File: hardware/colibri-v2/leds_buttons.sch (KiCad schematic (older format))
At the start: 38 parts

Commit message: added wnd_lcd.sch
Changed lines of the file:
@@
 $Descr A4 11693 8268
 encoding utf-8
-Sheet 4 22
+Sheet 4 23
 Title ""
 Date ""
@@
 	3100 2950 3250 2950
 Wire Wire Line
-	3250 2600 3250 2950
-Wire Wire Line
-	3250 2950 3250 3100
+	3250 2600 3250 3100
 $Comp
 L C C?
@@
 	2350 3850 2350 3600
 Wire Wire Line
-	2050 2950 2350 2950
-Wire Wire Line
-	2350 2950 2500 2950
+	2050 2950 2500 2950
 Wire Wire Line
 	2350 3300 2350 2950
@@
 	3100 4750 3250 4750
 Wire Wire Line
-	3250 4400 3250 4750
-Wire Wire Line
-	3250 4750 3250 4900
+	3250 4400 3250 4900
 $Comp
 L C C?
@@
 	2350 5650 2350 5400
 Wire Wire Line
-	2050 4750 2350 4750
-Wire Wire Line
-	2350 4750 2500 4750
+	2050 4750 2500 4750
 Wire Wire Line
 	2350 5100 2350 4750
@@
 	3100 6600 3250 6600
 Wire Wire Line
-	3250 6250 3250 6600
-Wire Wire Line
-	3250 6600 3250 6750
+	3250 6250 3250 6750
 $Comp
 L C C?
@@
 	2350 7500 2350 7250
 Wire Wire Line
-	2050 6600 2350 6600
-Wire Wire Line
-	2350 6600 2500 6600
+	2050 6600 2500 6600
 Wire Wire Line
 	2350 6950 2350 6600
@@
 	6050 2950 6200 2950
 Wire Wire Line
-	6200 2600 6200 2950
-Wire Wire Line
-	6200 2950 6200 3100
+	6200 2600 6200 3100
 $Comp
 L C C?
@@
 	5300 3850 5300 3600
 Wire Wire Line
-	5000 2950 5300 2950
-Wire Wire Line
-	5300 2950 5450 2950
+	5000 2950 5450 2950
 Wire Wire Line
 	5300 3300 5300 2950
@@
 	6050 4750 6200 4750
 Wire Wire Line
-	6200 4400 6200 4750
-Wire Wire Line
-	6200 4750 6200 4900
+	6200 4400 6200 4900
 $Comp
 L C C?
@@
 	5300 5650 5300 5400
 Wire Wire Line
-	5000 4750 5300 4750
-Wire Wire Line
-	5300 4750 5450 4750
+	5000 4750 5450 4750
 Wire Wire Line
 	5300 5100 5300 4750
@@
 	3250 1200 3100 1200
 Wire Wire Line
-	2350 1100 2350 1200
-Wire Wire Line
-	2350 1200 2350 1300
-Wire Wire Line
-	1350 1200 2350 1200
-Wire Wire Line
-	2350 1200 2500 1200
+	2350 1100 2350 1300
+Wire Wire Line
+	1350 1200 2500 1200
 Connection ~ 2350 1200
 Wire Wire Line
@@
 $EndComp
 Wire Wire Line
-	10100 850  10100 1150
-Wire Wire Line
-	10100 1150 10100 1450
-Wire Wire Line
-	10100 1450 10100 1750
-Wire Wire Line
-	10100 1750 10100 1950
+	10100 850  10100 1950
 Wire Wire Line
 	10100 850  9650 850
@@
 	5300 1200 5300 1300
 Wire Wire Line
-	4300 1200 5300 1200
-Wire Wire Line
-	5300 1200 5450 1200
+	4300 1200 5450 1200
 Connection ~ 5300 1200
 Text HLabel 4300 1200 0    60   Output ~ 0

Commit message: Annotated Components
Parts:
- gave numbers to parts that had none: 38

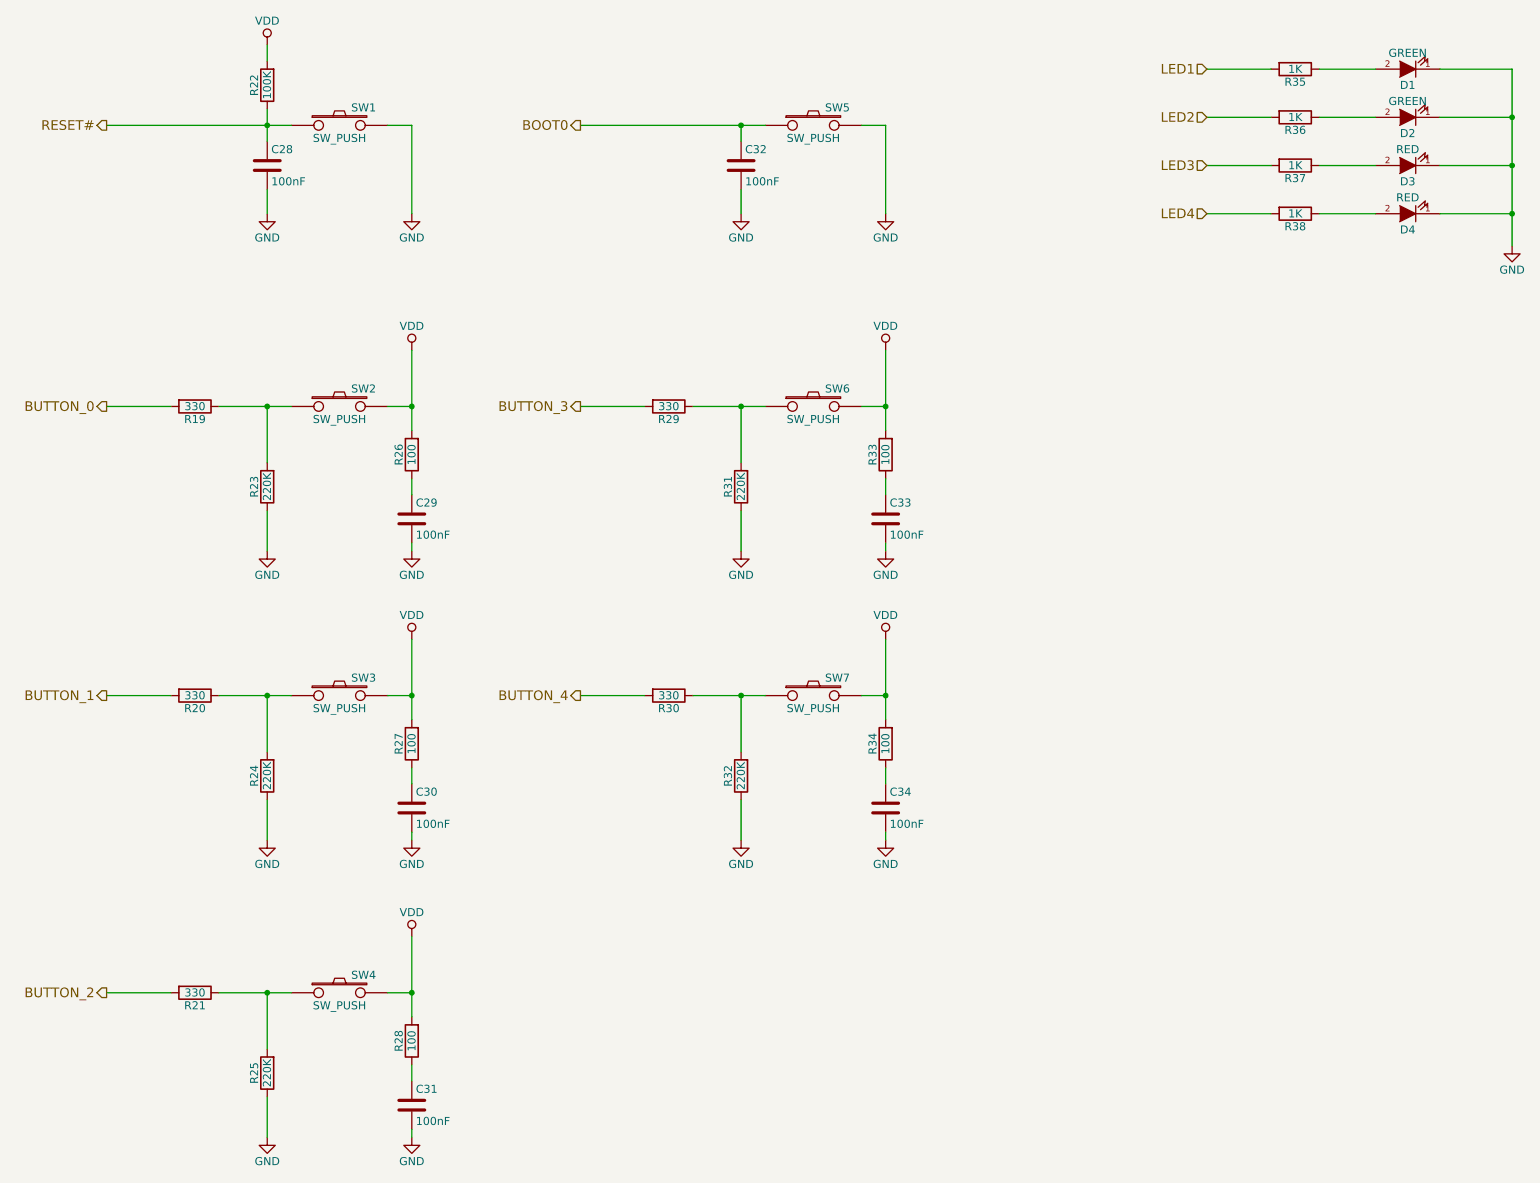
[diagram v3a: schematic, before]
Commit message: Changes in the button sheet
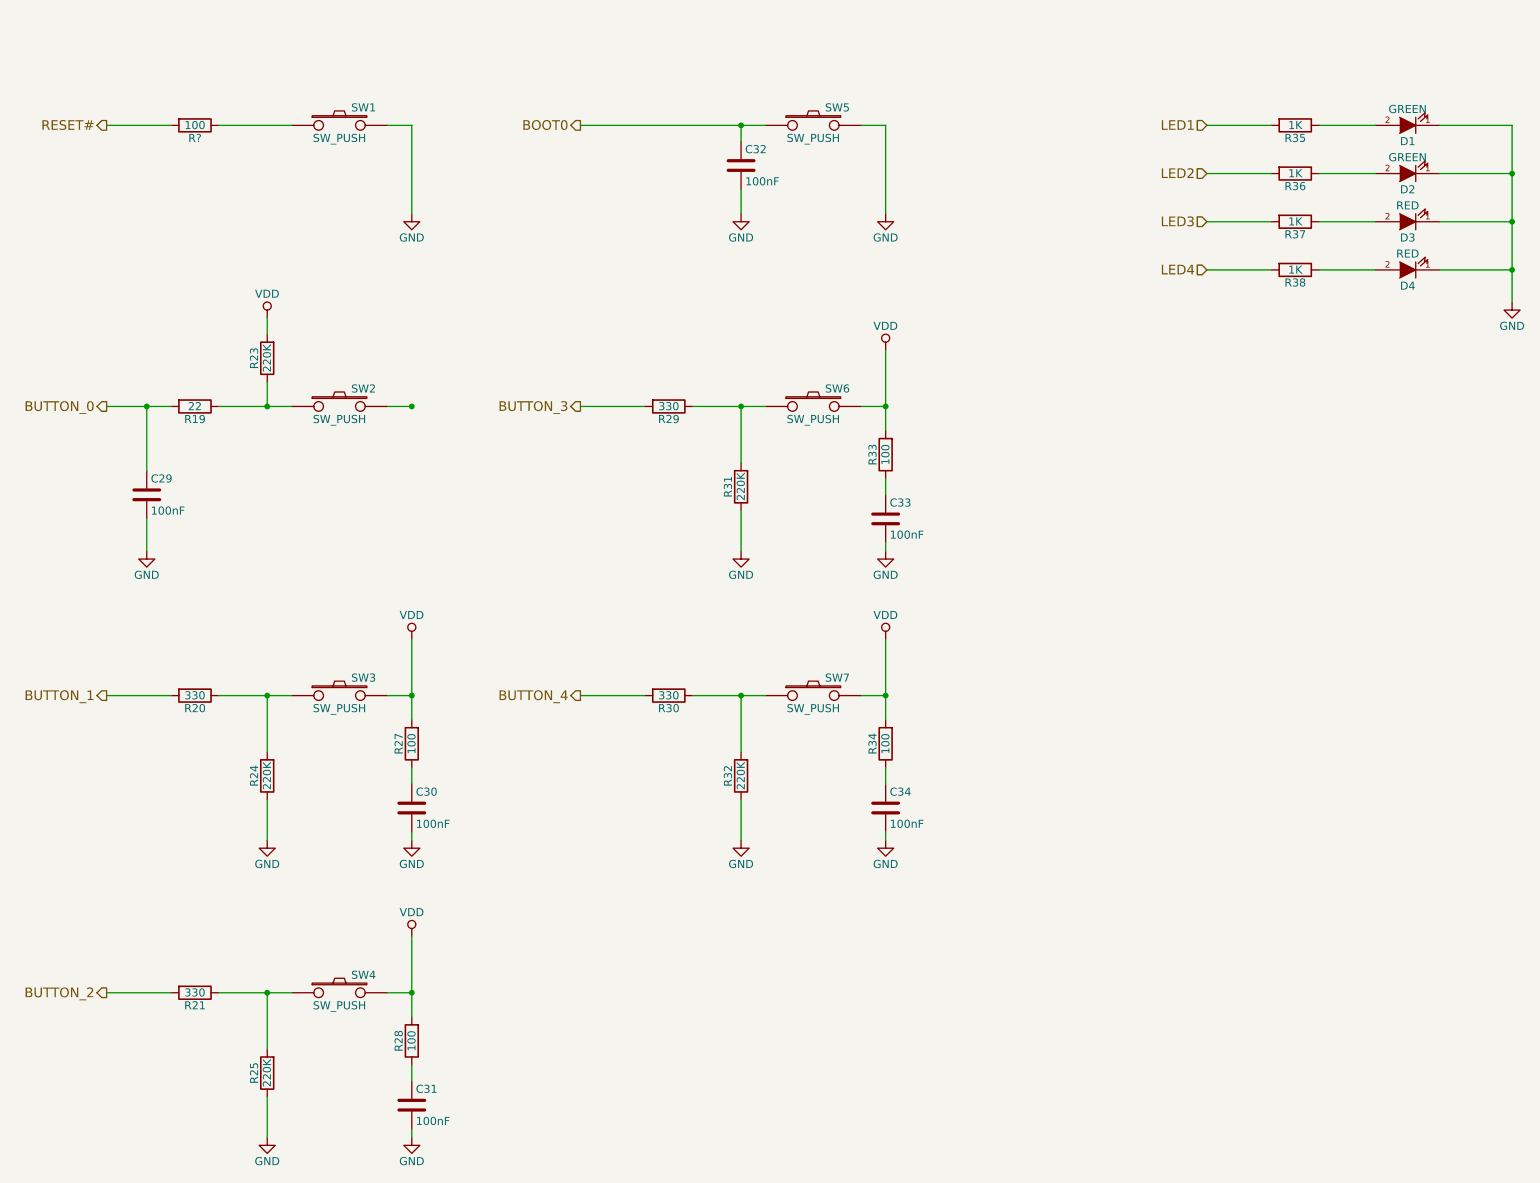
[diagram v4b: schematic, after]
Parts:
- removed C28: 100nF, symbol C
- removed R22: 100K, symbol R
- removed R26: 100, symbol R
- added R?: 100, symbol R
- R19: value 330 -> 22
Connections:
- net BUTTON_0: now also C29.1
- net GND: no longer R23.1
- net RESET#: now also R?.2; no longer SW1.1
- net VDD: now also R23.2; no longer SW2.2
- net at R19.1, SW2.1: now also R23.1; no longer R23.2
- new net: R?.1, SW1.1
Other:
- moved on the sheet: C29, D1, D2, D3, D4, R23, R35, R36, R37, R38

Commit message: Changes the leds
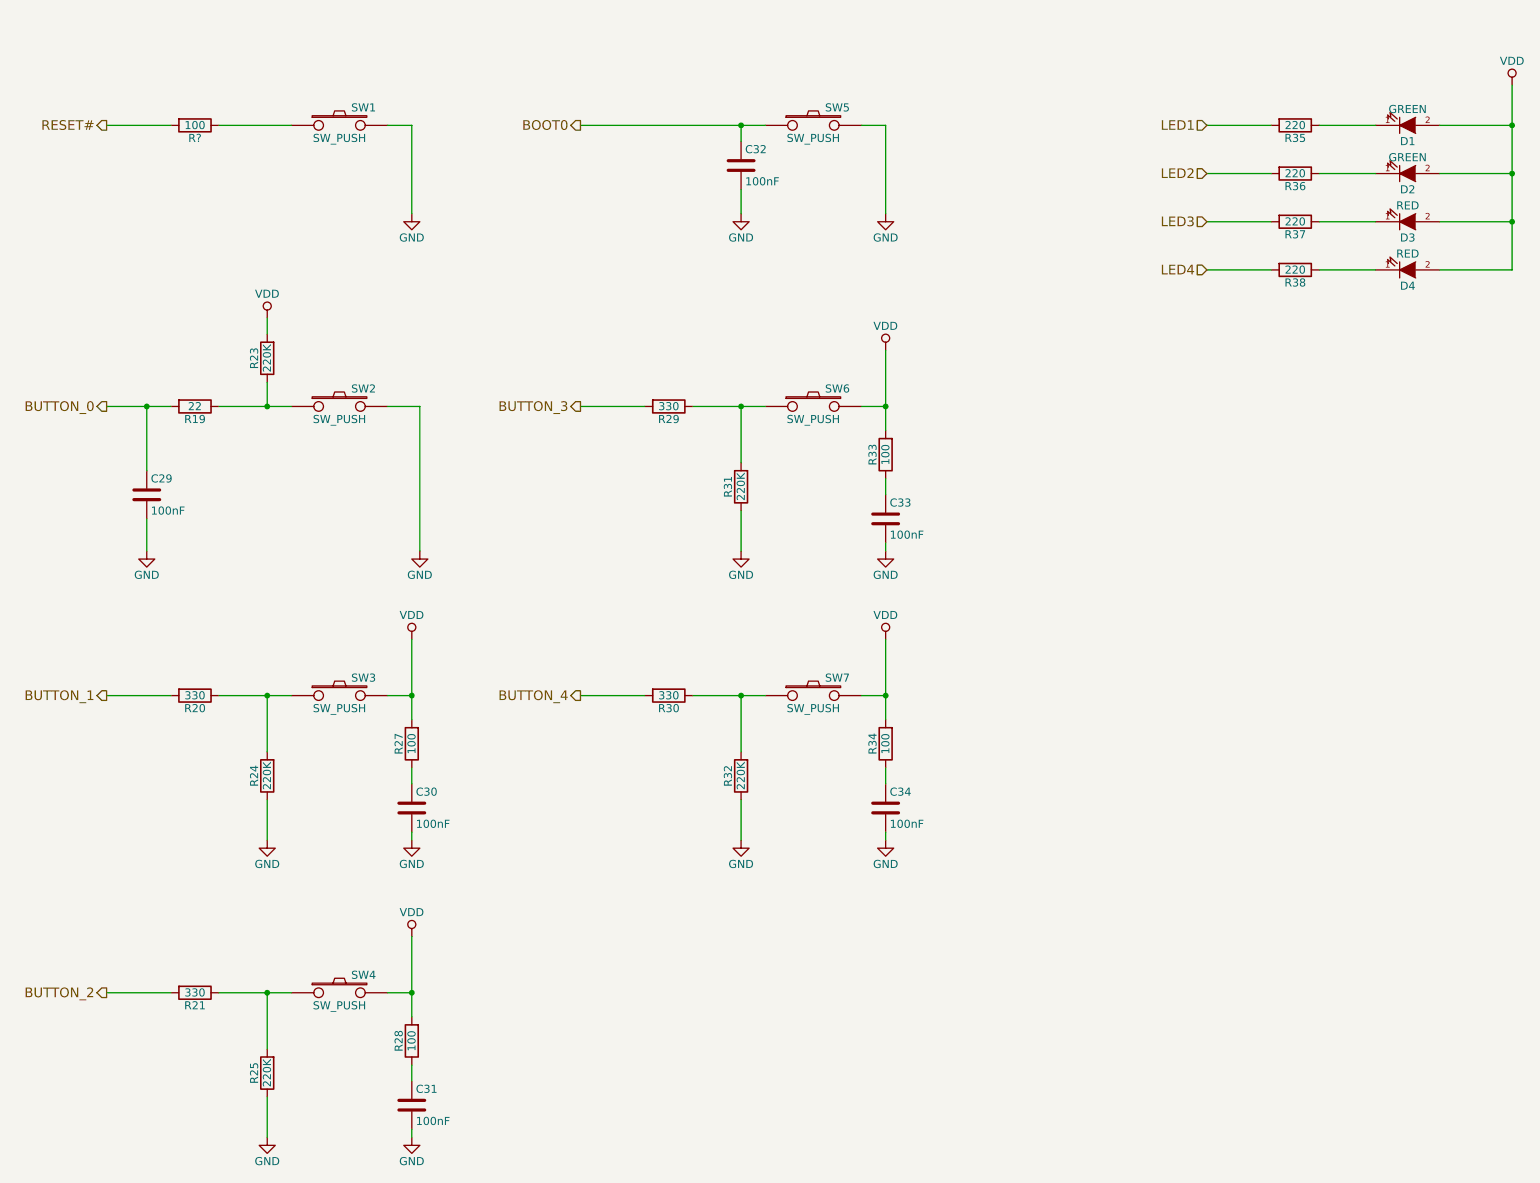
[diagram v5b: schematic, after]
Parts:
- R35, R36, R37, R38: value 1K -> 220
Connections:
- net GND: now also SW2.2; no longer D1.1 (K), D2.1 (K), D3.1 (K), D4.1 (K)
- net VDD: now also D1.2 (A), D2.2 (A), D3.2 (A), D4.2 (A)
- net at R35.1: now also D1.1 (K); no longer D1.2 (A)
- net at R36.1: now also D2.1 (K); no longer D2.2 (A)
- net at R37.1: now also D3.1 (K); no longer D3.2 (A)
- net at R38.1: now also D4.1 (K); no longer D4.2 (A)
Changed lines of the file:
@@
 	-1   0    0    1
 $EndComp
-Wire Wire Line
-	3100 2950 3250 2950
 $Comp
 L C C29
@@
 Wire Wire Line
 	1600 3850 1600 3650
-Connection ~ 3250 2950
-Wire Wire Line
-	2050 2950 2350 2950
-Wire Wire Line
-	2350 2950 2500 2950
+Wire Wire Line
+	2050 2950 2500 2950
 Connection ~ 2350 2950
 Wire Wire Line
-	1750 2950 1600 2950
-Wire Wire Line
-	1600 2950 1350 2950
+	1350 2950 1750 2950
 $Comp
 L SW_PUSH SW3
@@
 	3100 4750 3250 4750
 Wire Wire Line
-	3250 4400 3250 4750
-Wire Wire Line
-	3250 4750 3250 4900
+	3250 4400 3250 4900
 $Comp
 L C C30
@@
 	2350 5650 2350 5400
 Wire Wire Line
-	2050 4750 2350 4750
-Wire Wire Line
-	2350 4750 2500 4750
+	2050 4750 2500 4750
 Wire Wire Line
 	2350 5100 2350 4750
@@
 	3100 6600 3250 6600
 Wire Wire Line
-	3250 6250 3250 6600
-Wire Wire Line
-	3250 6600 3250 6750
+	3250 6250 3250 6750
 $Comp
 L C C31
@@
 	2350 7500 2350 7250
 Wire Wire Line
-	2050 6600 2350 6600
-Wire Wire Line
-	2350 6600 2500 6600
+	2050 6600 2500 6600
 Wire Wire Line
 	2350 6950 2350 6600
@@
 	6050 2950 6200 2950
 Wire Wire Line
-	6200 2600 6200 2950
-Wire Wire Line
-	6200 2950 6200 3100
+	6200 2600 6200 3100
 $Comp
 L C C33
@@
 	5300 3850 5300 3600
 Wire Wire Line
-	5000 2950 5300 2950
-Wire Wire Line
-	5300 2950 5450 2950
+	5000 2950 5450 2950
 Wire Wire Line
 	5300 3300 5300 2950
@@
 	6050 4750 6200 4750
 Wire Wire Line
-	6200 4400 6200 4750
-Wire Wire Line
-	6200 4750 6200 4900
+	6200 4400 6200 4900
 $Comp
 L C C34
@@
 	5300 5650 5300 5400
 Wire Wire Line
-	5000 4750 5300 4750
-Wire Wire Line
-	5300 4750 5450 4750
+	5000 4750 5450 4750
 Wire Wire Line
 	5300 5100 5300 4750
@@
 F 3 "" H 9450 1200 60  0000 C CNN
 	1    9450 1200
-	-1   0    0    1
+	1    0    0    1
 $EndComp
 $Comp
@@
 F 3 "" H 9450 1500 60  0000 C CNN
 	1    9450 1500
-	-1   0    0    1
+	1    0    0    1
 $EndComp
 $Comp
@@
 F 3 "" H 9450 1800 60  0000 C CNN
 	1    9450 1800
-	-1   0    0    1
+	1    0    0    1
 $EndComp
 $Comp
@@
 F 3 "" H 9450 2100 60  0000 C CNN
 	1    9450 2100
-	-1   0    0    1
+	1    0    0    1
 $EndComp
 $Comp
@@
 P 8750 1200
 F 0 "R35" V 8830 1200 50  0000 C CNN
-F 1 "1K" V 8750 1200 50  0000 C CNN
+F 1 "220" V 8750 1200 50  0000 C CNN
 F 2 "" V 8680 1200 30  0000 C CNN
 F 3 "" H 8750 1200 30  0000 C CNN
@@
 P 8750 1500
 F 0 "R36" V 8830 1500 50  0000 C CNN
-F 1 "1K" V 8750 1500 50  0000 C CNN
+F 1 "220" V 8750 1500 50  0000 C CNN
 F 2 "" V 8680 1500 30  0000 C CNN
 F 3 "" H 8750 1500 30  0000 C CNN
@@
 P 8750 1800
 F 0 "R37" V 8830 1800 50  0000 C CNN
-F 1 "1K" V 8750 1800 50  0000 C CNN
+F 1 "220" V 8750 1800 50  0000 C CNN
 F 2 "" V 8680 1800 30  0000 C CNN
 F 3 "" H 8750 1800 30  0000 C CNN
@@
 P 8750 2100
 F 0 "R38" V 8830 2100 50  0000 C CNN
-F 1 "1K" V 8750 2100 50  0000 C CNN
+F 1 "220" V 8750 2100 50  0000 C CNN
 F 2 "" V 8680 2100 30  0000 C CNN
 F 3 "" H 8750 2100 30  0000 C CNN
@@
 	0    1    1    0
 $EndComp
-$Comp
-L GND #PWR38
-U 1 1 558636BC
-P 10100 2300
-F 0 "#PWR38" H 10100 2050 50  0001 C CNN
-F 1 "GND" H 10100 2150 50  0000 C CNN
-F 2 "" H 10100 2300 60  0000 C CNN
-F 3 "" H 10100 2300 60  0000 C CNN
-	1    10100 2300
-	1    0    0    -1
-$EndComp
-Wire Wire Line
-	10100 1200 10100 1500
-Wire Wire Line
-	10100 1500 10100 1800
-Wire Wire Line
-	10100 1800 10100 2100
-Wire Wire Line
-	10100 2100 10100 2300
 Wire Wire Line
 	10100 1200 9650 1200
@@
 Connection ~ 10100 1800
 Wire Wire Line
-	9650 2100 10100 2100
-Connection ~ 10100 2100
+	10100 2100 9650 2100
 Wire Wire Line
 	8900 1200 9250 1200
@@
 	5300 1200 5300 1300
 Wire Wire Line
-	4300 1200 5300 1200
-Wire Wire Line
-	5300 1200 5450 1200
+	4300 1200 5450 1200
 Connection ~ 5300 1200
 Text HLabel 4300 1200 0    60   Output ~ 0
@@
 	1600 3350 1600 2950
 Connection ~ 1600 2950
+$Comp
+L GND #PWR?
+U 1 1 5622B260
+P 3300 3850
+F 0 "#PWR?" H 3300 3600 50  0001 C CNN
+F 1 "GND" H 3300 3700 50  0000 C CNN
+F 2 "" H 3300 3850 60  0000 C CNN
+F 3 "" H 3300 3850 60  0000 C CNN
+	1    3300 3850
+	1    0    0    -1
+$EndComp
+Wire Wire Line
+	3100 2950 3300 2950
+Wire Wire Line
+	3300 2950 3300 3850
+Wire Wire Line
+	10100 950  10100 2100
+$Comp
+L VDD #PWR?
+U 1 1 5622B87E
+P 10100 950
+F 0 "#PWR?" H 10100 800 50  0001 C CNN
+F 1 "VDD" H 10100 1100 50  0000 C CNN
+F 2 "" H 10100 950 60  0000 C CNN
+F 3 "" H 10100 950 60  0000 C CNN
+	1    10100 950
+	1    0    0    -1
+$EndComp
+Connection ~ 10100 1200
 $EndSCHEMATC
